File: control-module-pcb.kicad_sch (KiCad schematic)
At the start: 2 parts, among them J3 Power Outputs, J4 Ignition Outputs

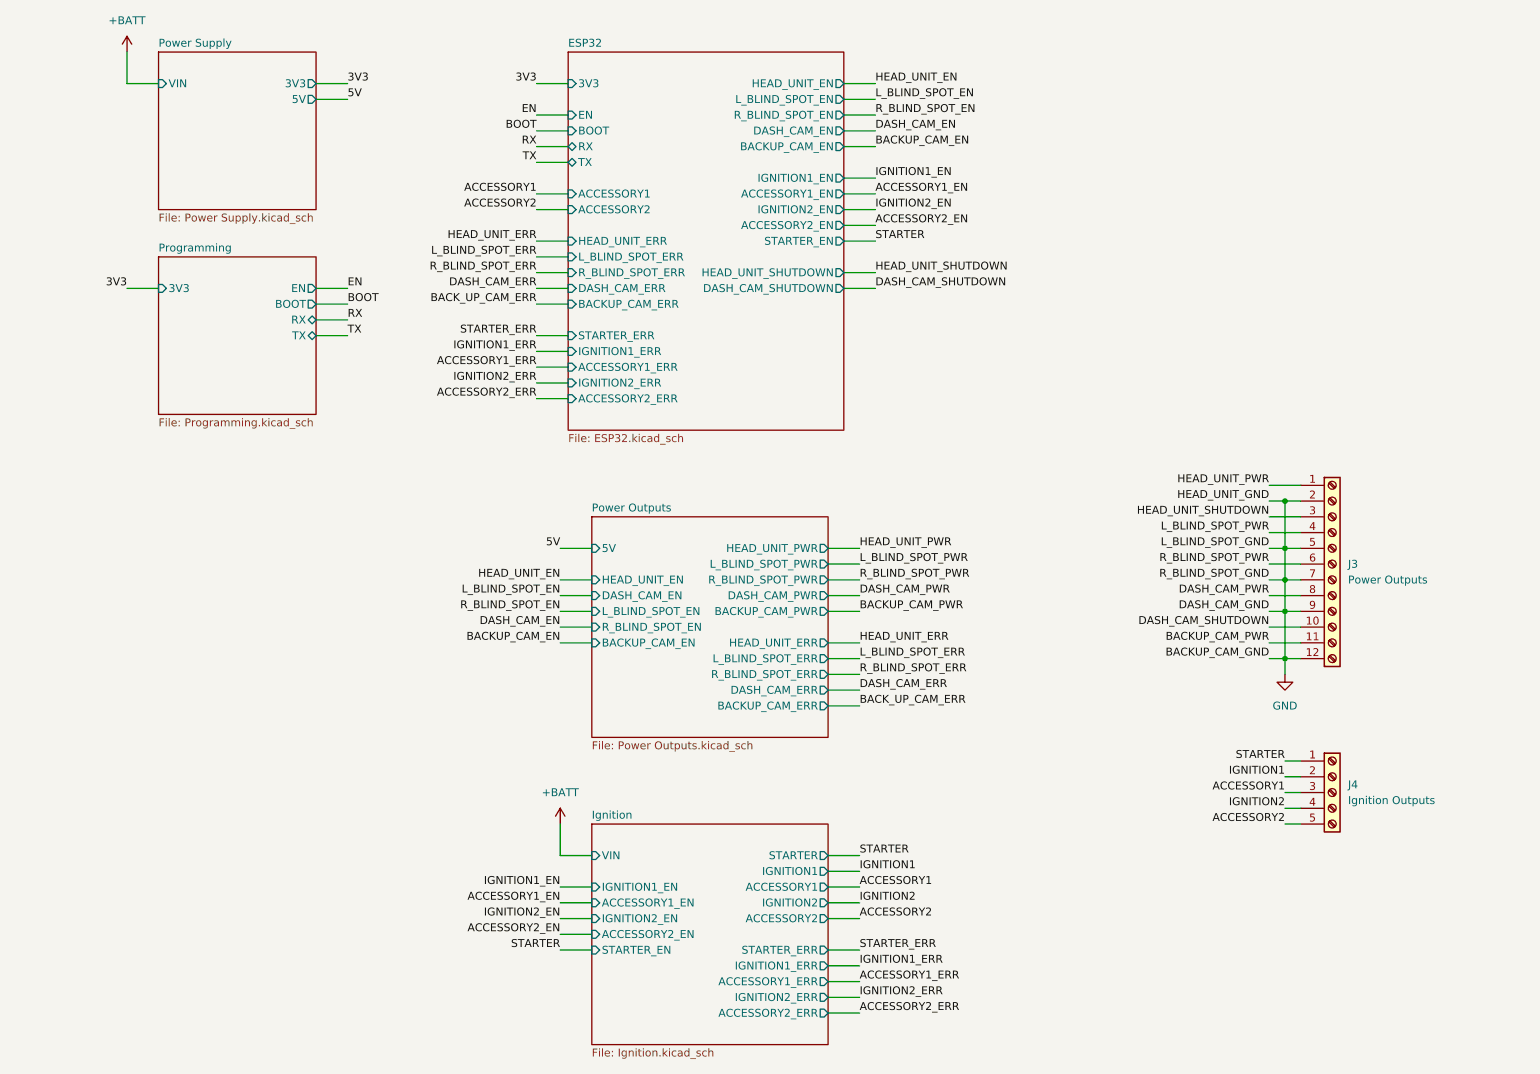
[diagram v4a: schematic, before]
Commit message: finished assigning footprints and started PCB layout
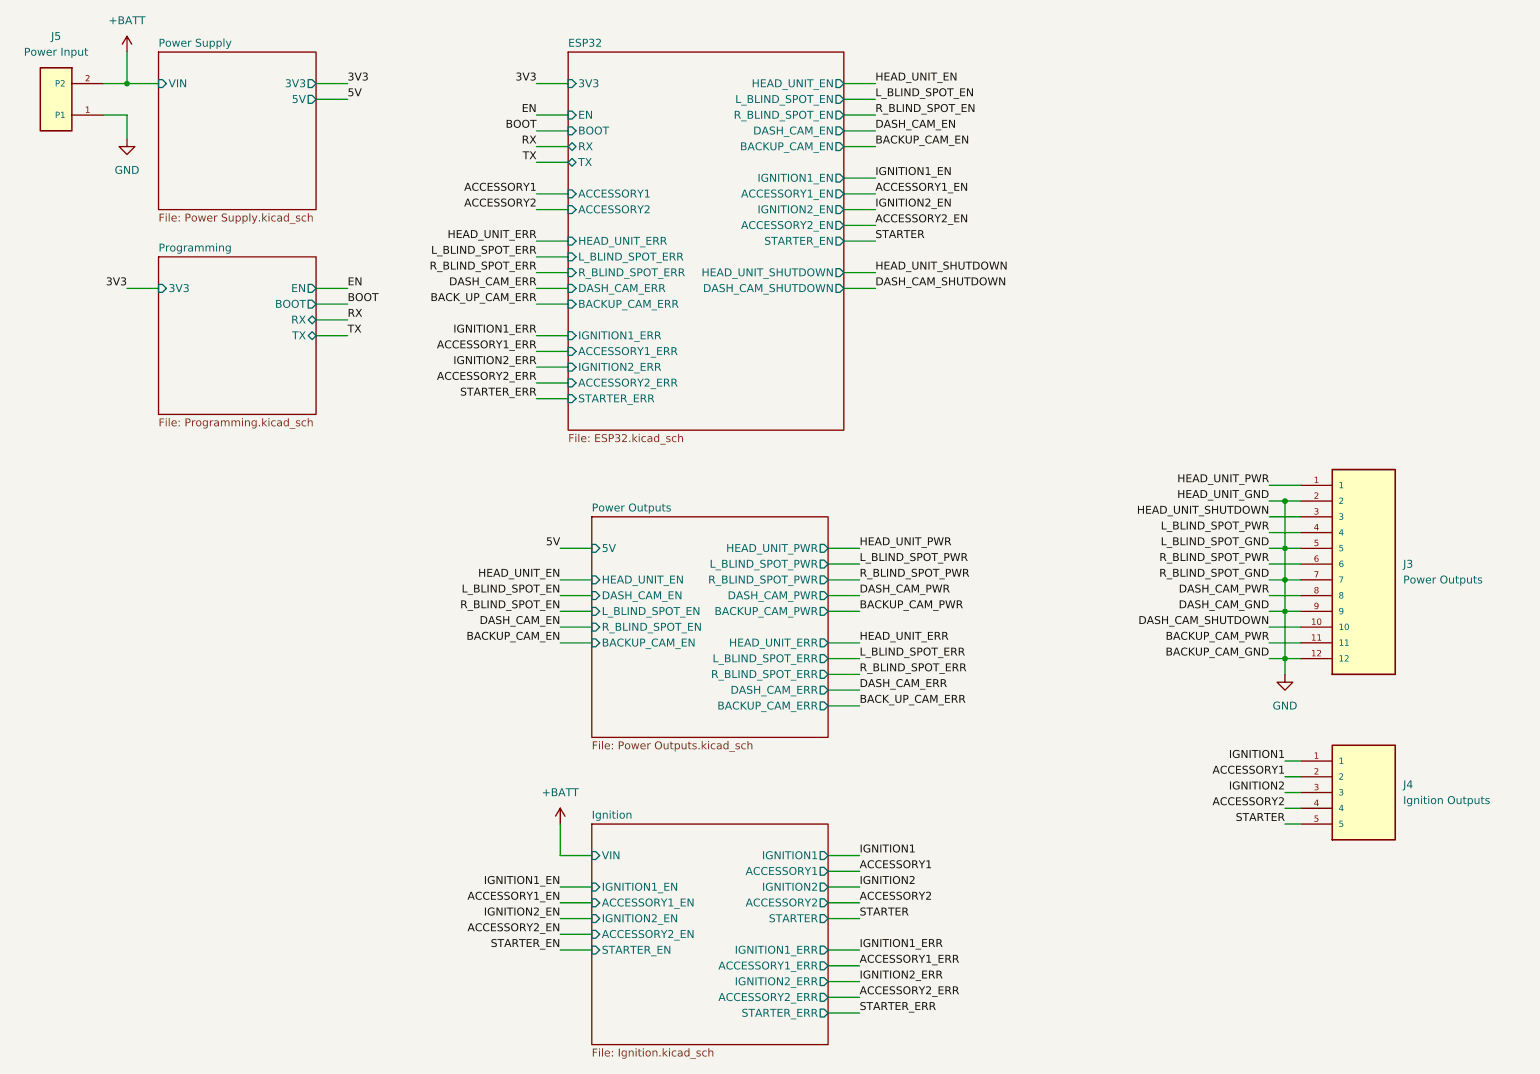
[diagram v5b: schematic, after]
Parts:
- removed J3: Power Outputs, symbol Connector:Screw_Terminal_01x12
- removed J4: Ignition Outputs, symbol Connector:Screw_Terminal_01x05
- added J3: Power Outputs, 1-1776275-2:TE_1-1776275-2, symbol 1-1776275-2:1-1776275-2
- added J4: Ignition Outputs, 1776275-5:TE_1776275-5, symbol 1776275-5:1776275-5
- added J5: Power Input, 1776275-2:TE_1776275-2, symbol 1776275-2:1776275-2
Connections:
- net +BATT: now also J5.2 (P2)
- net ACCESSORY1: now also J4.2
- net ACCESSORY2: now also J4.4
- net BACKUP_CAM_PWR: now also J3.11
- net DASH_CAM_PWR: now also J3.8
- net DASH_CAM_SHUTDOWN: now also J3.10
- net GND: now also J3.12, J3.2, J3.5, J3.7, J3.9, J5.1 (P1)
- net HEAD_UNIT_PWR: now also J3.1
- net HEAD_UNIT_SHUTDOWN: now also J3.3
- net IGNITION1: now also J4.1
- net IGNITION2: now also J4.3
- net L_BLIND_SPOT_PWR: now also J3.4
- net R_BLIND_SPOT_PWR: now also J3.6
- net STARTER: now also J4.5
